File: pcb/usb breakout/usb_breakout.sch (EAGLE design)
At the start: 5 parts

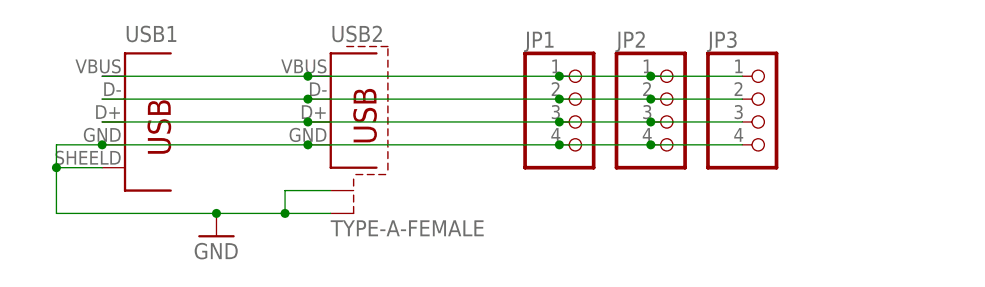
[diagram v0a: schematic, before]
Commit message: updated usb breakout board
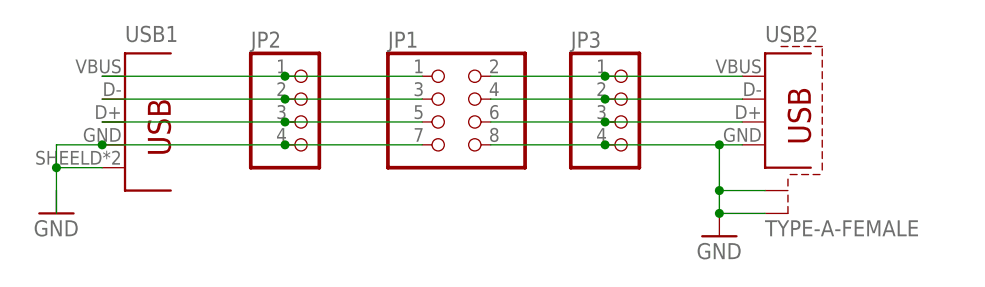
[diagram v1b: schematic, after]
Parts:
- JP1: device pinhead:PINHD-1X4 -> pinhead:PINHD-2X4
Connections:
- new net N$4: JP1.2, JP3.1, USB2.VCC
- new net N$5: JP1.4, JP3.2, USB2.D-
- new net N$6: JP1.6, JP3.3, USB2.D+
- net GND: now also JP1.7, JP1.8; no longer JP1.4
- net N$1: no longer JP3.1, USB2.VCC
- net N$2: now also JP1.3; no longer JP1.2, JP3.2, USB2.D-
- net N$3: now also JP1.5; no longer JP1.3, JP3.3, USB2.D+
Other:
- moved on the sheet: JP2, JP3, USB1, USB2
